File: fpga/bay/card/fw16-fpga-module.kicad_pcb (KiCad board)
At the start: 2 copper layers, 0 parts

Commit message: card PCB: 8-layer 1.2 mm stackup, outline from card-outline.dxf (holes on Dwgs.User), 201 footprints from the schematic; J1 at origin, U14 (rot 90, GT edge to the interposer), H1-H4 per 0012
Co-Authored-By: Claude Opus 5.5 (1M context) <noreply@anthropic.com>
Claude-Session: https://claude.ai/code/session_019QA2U79cSHCaAaMe6Km575
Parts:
- added C1: 10u/25V, Capacitor_SMD:C_1206_3216Metric, F.Cu at (7.30, 28.8)
- added C10: 10u/25V, Capacitor_SMD:C_1206_3216Metric, F.Cu at (7.30, 324.6)
- added C11: 100n/25V, Capacitor_SMD:C_0402_1005Metric, F.Cu at (5.91, 331.2)
- added C12: 100n, Capacitor_SMD:C_0402_1005Metric, F.Cu at (5.91, 337.2)
- added C13: 1u, Capacitor_SMD:C_0402_1005Metric, F.Cu at (5.91, 343.2)
- added C14: 22u/16V, Capacitor_SMD:C_1206_3216Metric, F.Cu at (7.30, 349.9)
- added C15: 22u/16V, Capacitor_SMD:C_1206_3216Metric, F.Cu at (7.30, 357.2)
- added C16: 22u/16V, Capacitor_SMD:C_1206_3216Metric, F.Cu at (7.30, 364.5)
- added C17: 100n, Capacitor_SMD:C_0402_1005Metric, F.Cu at (5.91, 893.7)
- added C18: 100n, Capacitor_SMD:C_0402_1005Metric, F.Cu at (5.91, 500.3)
- added C19: 10u/10V, Capacitor_SMD:C_0805_2012Metric, F.Cu at (6.70, 506.8)
- added C2: 100n, Capacitor_SMD:C_0402_1005Metric, F.Cu at (5.91, 56.0)
- added C20: 10u/10V, Capacitor_SMD:C_0805_2012Metric, F.Cu at (6.70, 513.7)
- added C21: 100n, Capacitor_SMD:C_0402_1005Metric, F.Cu at (5.91, 520.2)
- added C22: 100n, Capacitor_SMD:C_0402_1005Metric, F.Cu at (5.91, 526.2)
- added C23: 1u, Capacitor_SMD:C_0402_1005Metric, F.Cu at (5.91, 532.2)
- added C24: 22u/6.3V, Capacitor_SMD:C_0805_2012Metric, F.Cu at (6.70, 538.7)
- added C25: 22u/6.3V, Capacitor_SMD:C_0805_2012Metric, F.Cu at (6.70, 545.7)
- added C26: 22u/6.3V, Capacitor_SMD:C_0805_2012Metric, F.Cu at (6.70, 552.6)
- added C27: 22u/6.3V, Capacitor_SMD:C_0805_2012Metric, F.Cu at (6.70, 559.6)
- added C28: 10u/10V, Capacitor_SMD:C_0805_2012Metric, F.Cu at (6.70, 566.5)
- added C29: 22u/6.3V, Capacitor_SMD:C_0805_2012Metric, F.Cu at (6.70, 573.5)
- added C3: 1u/25V, Capacitor_SMD:C_0603_1608Metric, F.Cu at (6.48, 279.1)
- added C30: 10u/10V, Capacitor_SMD:C_0805_2012Metric, F.Cu at (6.70, 580.5)
- added C31: 22u/6.3V, Capacitor_SMD:C_0805_2012Metric, F.Cu at (6.70, 587.4)
- added C32: 1u/10V, Capacitor_SMD:C_0402_1005Metric, F.Cu at (5.91, 593.9)
- added C33: 1u, Capacitor_SMD:C_0402_1005Metric, F.Cu at (5.91, 599.9)
- added C34: 1u/10V, Capacitor_SMD:C_0402_1005Metric, F.Cu at (5.91, 605.9)
- added C35: 1u, Capacitor_SMD:C_0402_1005Metric, F.Cu at (5.91, 611.9)
- added C36: 10u/10V, Capacitor_SMD:C_0805_2012Metric, F.Cu at (6.70, 618.4)
- added C37: 1u/10V, Capacitor_SMD:C_0402_1005Metric, F.Cu at (5.91, 624.9)
- added C38: 10n, Capacitor_SMD:C_0402_1005Metric, F.Cu at (5.91, 630.9)
- added C39: 47u/6.3V, Capacitor_SMD:C_1206_3216Metric, F.Cu at (7.30, 637.5)
- added C4: 100n/25V, Capacitor_SMD:C_0402_1005Metric, F.Cu at (5.91, 285.3)
- added C40: 10u/6.3V, Capacitor_SMD:C_0805_2012Metric, F.Cu at (6.70, 644.6)
- added C41: 10u/10V, Capacitor_SMD:C_0805_2012Metric, F.Cu at (6.70, 651.6)
- added C42: 1u/10V, Capacitor_SMD:C_0402_1005Metric, F.Cu at (5.91, 658.1)
- added C43: 10n, Capacitor_SMD:C_0402_1005Metric, F.Cu at (5.91, 664.1)
- added C44: 47u/6.3V, Capacitor_SMD:C_1206_3216Metric, F.Cu at (7.30, 670.7)
- added C45: 10u/6.3V, Capacitor_SMD:C_0805_2012Metric, F.Cu at (6.70, 677.9)
- added C46: 330u/2.5V polymer, Capacitor_Tantalum_SMD:CP_EIA-7343-31_Kemet-D, F.Cu at (9.41, 983.8)
- added C47: 100u/4V, Capacitor_SMD:C_1210_3225Metric, F.Cu at (7.30, 992.8)
- added C48: 47u/4V, Capacitor_SMD:C_1206_3216Metric, F.Cu at (7.30, 1000.6)
- added C49: 47u/4V, Capacitor_SMD:C_1206_3216Metric, F.Cu at (7.30, 1007.9)
- added C5: 10n, Capacitor_SMD:C_0402_1005Metric, F.Cu at (5.91, 291.3)
- added C50: 10u/4V, Capacitor_SMD:C_0603_1608Metric, F.Cu at (6.48, 1014.8)
- added C51: 10u/4V, Capacitor_SMD:C_0603_1608Metric, F.Cu at (6.48, 1021.2)
- added C52: 100n, Capacitor_SMD:C_0402_1005Metric, F.Cu at (5.91, 1027.4)
- added C53: 100n, Capacitor_SMD:C_0402_1005Metric, F.Cu at (5.91, 1033.4)
- added C54: 100n, Capacitor_SMD:C_0402_1005Metric, F.Cu at (5.91, 1039.4)
- added C55: 100n, Capacitor_SMD:C_0402_1005Metric, F.Cu at (5.91, 1045.4)
- added C56: 100n, Capacitor_SMD:C_0402_1005Metric, F.Cu at (5.91, 1051.4)
- added C57: 100n, Capacitor_SMD:C_0402_1005Metric, F.Cu at (5.91, 1057.4)
- added C58: 100n, Capacitor_SMD:C_0402_1005Metric, F.Cu at (5.91, 1063.4)
- added C59: 100n, Capacitor_SMD:C_0402_1005Metric, F.Cu at (5.91, 1069.4)
- added C6: 2.2n, Capacitor_SMD:C_0402_1005Metric, F.Cu at (5.91, 297.3)
- added C60: 47u/4V, Capacitor_SMD:C_1206_3216Metric, F.Cu at (7.30, 1076.1)
- added C61: 10u/4V, Capacitor_SMD:C_0603_1608Metric, F.Cu at (6.48, 1083.0)
- added C62: 10u/4V, Capacitor_SMD:C_0603_1608Metric, F.Cu at (6.48, 1089.4)
- added C63: 47u/4V, Capacitor_SMD:C_1206_3216Metric, F.Cu at (7.30, 1096.3)
- added C64: 47u/4V, Capacitor_SMD:C_1206_3216Metric, F.Cu at (7.30, 1103.6)
- added C65: 10u/4V, Capacitor_SMD:C_0603_1608Metric, F.Cu at (6.48, 1110.5)
- added C66: 10u/4V, Capacitor_SMD:C_0603_1608Metric, F.Cu at (6.48, 1117.0)
- added C67: 10u/4V, Capacitor_SMD:C_0603_1608Metric, F.Cu at (6.48, 1123.4)
- added C68: 10u/4V, Capacitor_SMD:C_0603_1608Metric, F.Cu at (6.48, 1129.9)
- added C69: 10u/4V, Capacitor_SMD:C_0603_1608Metric, F.Cu at (6.48, 1136.3)
- added C7: 10u/25V, Capacitor_SMD:C_1206_3216Metric, F.Cu at (7.30, 304.0)
- added C70: 47u/6.3V, Capacitor_SMD:C_1206_3216Metric, F.Cu at (7.30, 1143.2)
- added C71: 10u/6.3V, Capacitor_SMD:C_0603_1608Metric, F.Cu at (6.48, 1150.1)
- added C72: 4.7u/6.3V, Capacitor_SMD:C_0603_1608Metric, F.Cu at (6.48, 1156.6)
- added C73: 4.7u/6.3V, Capacitor_SMD:C_0603_1608Metric, F.Cu at (6.48, 1163.0)
- added C74: 4.7u/6.3V, Capacitor_SMD:C_0603_1608Metric, F.Cu at (6.48, 1169.5)
- added C75: 470n, Capacitor_SMD:C_0402_1005Metric, F.Cu at (5.91, 1175.7)
- added C76: 100n, Capacitor_SMD:C_0402_1005Metric, F.Cu at (5.91, 1181.7)
- added C77: 220n, Capacitor_SMD:C_0402_1005Metric, F.Cu at (5.91, 1187.7)
- added C78: 220n, Capacitor_SMD:C_0402_1005Metric, F.Cu at (5.91, 1193.7)
- added C79: 220n, Capacitor_SMD:C_0402_1005Metric, F.Cu at (5.91, 1199.7)
- added C8: 100n, Capacitor_SMD:C_0402_1005Metric, F.Cu at (5.91, 310.6)
- added C80: 220n, Capacitor_SMD:C_0402_1005Metric, F.Cu at (5.91, 1205.7)
- added C81: 220n, Capacitor_SMD:C_0402_1005Metric, F.Cu at (5.91, 1211.7)
- added C82: 220n, Capacitor_SMD:C_0402_1005Metric, F.Cu at (5.91, 1217.7)
- added C83: 220n, Capacitor_SMD:C_0402_1005Metric, F.Cu at (5.91, 1223.7)
- added C84: 220n, Capacitor_SMD:C_0402_1005Metric, F.Cu at (5.91, 1229.7)
- added C85: 10n, Capacitor_SMD:C_0402_1005Metric, F.Cu at (5.91, 1235.7)
- added C86: 10n, Capacitor_SMD:C_0402_1005Metric, F.Cu at (5.91, 1241.7)
- added C87: 100n, Capacitor_SMD:C_0402_1005Metric, F.Cu at (5.91, 1247.7)
- added C88: 100n DNP, Capacitor_SMD:C_0402_1005Metric, F.Cu at (5.91, 1253.7)
- added C89: 10n DNP, Capacitor_SMD:C_0402_1005Metric, F.Cu at (5.91, 1259.7)
- added C9: 10u/25V, Capacitor_SMD:C_1206_3216Metric, F.Cu at (7.30, 317.3)
- added C90: 10n DNP, Capacitor_SMD:C_0402_1005Metric, F.Cu at (5.91, 1265.7)
- added D1: green, LED_SMD:LED_0603_1608Metric, F.Cu at (6.48, 1271.9)
- added D2: green, LED_SMD:LED_0603_1608Metric, F.Cu at (6.48, 1278.4)
- added FB1: BLM18PG221SN1, Inductor_SMD:L_0603_1608Metric, F.Cu at (6.48, 1284.9)
- added FB2: BLM18PG221SN1, Inductor_SMD:L_0603_1608Metric, F.Cu at (6.48, 1291.3)
- added H1: M2 SMT nut 9774030243R, fw16-fpga-module:Wurth_WA-SMSI_M2_9774030243R, F.Cu at (-17.5, -52.0)
- added H2: M2 SMT nut 9774030243R, fw16-fpga-module:Wurth_WA-SMSI_M2_9774030243R, F.Cu at (17.5, -52.0)
- added H3: M2 SMT nut 9774030243R, fw16-fpga-module:Wurth_WA-SMSI_M2_9774030243R, F.Cu at (-17.5, -30.1)
- added H4: M2 SMT nut 9774030243R, fw16-fpga-module:Wurth_WA-SMSI_M2_9774030243R, F.Cu at (17.5, -30.1)
- added J1: FXBeam_2x74_DB, fw16-fpga-module:FXBeam_2x74_DB, F.Cu at (0.00, 0.00)
- added J2: AFC58-S04FIA-R1, fw16-fpga-module:AFC58-S04FIA-R1, F.Cu at (8.60, 37.6)
- added J3: AFC58-S04FIA-R1, fw16-fpga-module:AFC58-S04FIA-R1, F.Cu at (8.60, 47.9)
- added J4: TC2050-IDC-NL (Xilinx), Connector:Tag-Connect_TC2050-IDC-NL_2x05_P1.27mm_Vertical, F.Cu at (11.2, 902.6)
- added J5: U.FL PPS/10MHz/trigger, Connector_Coaxial:U.FL_Hirose_U.FL-R-SMT-1_Vertical, F.Cu at (7.17, 1342.8)
- added JP1: WP_EN, Jumper:SolderJumper-2_P1.3mm_Open_Pad1.0x1.5mm, F.Cu at (6.65, 62.7)
- added L1: 10u XAL5030-103, Inductor_SMD:L_Coilcraft_XAL5030-XXX, F.Cu at (7.99, 373.7)
- added L2: 1u XAL4020-102, Inductor_SMD:L_Coilcraft_XAL4020-XXX, F.Cu at (7.40, 686.2)
- added L3: 2.2u DFE201610, Inductor_SMD:L_Murata_DFE201610P, F.Cu at (6.25, 694.7)
- added L4: 2.2u DFE201610, Inductor_SMD:L_Murata_DFE201610P, F.Cu at (6.25, 701.8)
- added Q1: 2N7002K, Package_TO_SOT_SMD:SOT-23, F.Cu at (6.93, 854.1)
- added Q2: 2N7002K, Package_TO_SOT_SMD:SOT-23, F.Cu at (6.93, 862.5)
- added R1: 330k, Resistor_SMD:R_0402_1005Metric, F.Cu at (5.93, 16.2)
- added R10: 1.33k, Resistor_SMD:R_0402_1005Metric, F.Cu at (5.93, 406.3)
- added R11: 390k, Resistor_SMD:R_0402_1005Metric, F.Cu at (5.93, 412.3)
- added R12: 91k, Resistor_SMD:R_0402_1005Metric, F.Cu at (5.93, 418.3)
- added R13: 10k, Resistor_SMD:R_0402_1005Metric, F.Cu at (5.93, 424.3)
- added R14: 10m 1%, Resistor_SMD:R_1206_3216Metric, F.Cu at (7.28, 430.9)
- added R15: 4.7k, Resistor_SMD:R_0402_1005Metric, F.Cu at (5.93, 437.5)
- added R16: 4.7k, Resistor_SMD:R_0402_1005Metric, F.Cu at (5.93, 443.5)
- added R17: 10k, Resistor_SMD:R_0402_1005Metric, F.Cu at (5.93, 449.5)
- added R18: 100k, Resistor_SMD:R_0402_1005Metric, F.Cu at (5.93, 455.5)
- added R19: 24.9k, Resistor_SMD:R_0402_1005Metric, F.Cu at (5.93, 461.5)
- added R2: 330k, Resistor_SMD:R_0402_1005Metric, F.Cu at (5.93, 22.2)
- added R20: 10k, Resistor_SMD:R_0402_1005Metric, F.Cu at (5.93, 467.5)
- added R21: 100k, Resistor_SMD:R_0402_1005Metric, F.Cu at (5.93, 869.7)
- added R22: 100k, Resistor_SMD:R_0402_1005Metric, F.Cu at (5.93, 875.7)
- added R23: 0R, Resistor_SMD:R_0402_1005Metric, F.Cu at (5.93, 881.7)
- added R24: 0R DNP, Resistor_SMD:R_0402_1005Metric, F.Cu at (5.93, 887.7)
- added R25: 2.4k, Resistor_SMD:R_0402_1005Metric, F.Cu at (5.93, 911.4)
- added R26: 4.7k, Resistor_SMD:R_0402_1005Metric, F.Cu at (5.93, 917.4)
- added R27: 4.7k, Resistor_SMD:R_0402_1005Metric, F.Cu at (5.93, 923.4)
- added R28: 4.7k, Resistor_SMD:R_0402_1005Metric, F.Cu at (5.93, 929.4)
- added R29: 4.7k, Resistor_SMD:R_0402_1005Metric, F.Cu at (5.93, 935.4)
- added R3: 10k, Resistor_SMD:R_0402_1005Metric, F.Cu at (5.93, 69.5)
- added R30: 4.7k, Resistor_SMD:R_0402_1005Metric, F.Cu at (5.93, 941.4)
- added R31: 1k, Resistor_SMD:R_0402_1005Metric, F.Cu at (5.93, 947.4)
- added R32: 1k, Resistor_SMD:R_0402_1005Metric, F.Cu at (5.93, 953.4)
- added R33: 1k, Resistor_SMD:R_0402_1005Metric, F.Cu at (5.93, 959.4)
- added R34: 1k, Resistor_SMD:R_0402_1005Metric, F.Cu at (5.93, 965.4)
- added R35: 100k, Resistor_SMD:R_0402_1005Metric, F.Cu at (5.93, 708.4)
- added R36: 100k, Resistor_SMD:R_0402_1005Metric, F.Cu at (5.93, 714.4)
- added R37: 100k, Resistor_SMD:R_0402_1005Metric, F.Cu at (5.93, 720.4)
- added R38: 8.45k 0.1%, Resistor_SMD:R_0402_1005Metric, F.Cu at (5.93, 726.4)
- added R39: 20k 0.1%, Resistor_SMD:R_0402_1005Metric, F.Cu at (5.93, 732.4)
- added R4: 2.2k DNP, Resistor_SMD:R_0402_1005Metric, F.Cu at (5.93, 75.5)
- added R40: 100k, Resistor_SMD:R_0402_1005Metric, F.Cu at (5.93, 738.4)
- added R41: 200k, Resistor_SMD:R_0402_1005Metric, F.Cu at (5.93, 744.4)
- added R42: 100k, Resistor_SMD:R_0402_1005Metric, F.Cu at (5.93, 750.4)
- added R43: 100k, Resistor_SMD:R_0402_1005Metric, F.Cu at (5.93, 756.4)
- added R44: 200k, Resistor_SMD:R_0402_1005Metric, F.Cu at (5.93, 762.4)
- added R45: 120k, Resistor_SMD:R_0402_1005Metric, F.Cu at (5.93, 768.4)
- added R46: 100k, Resistor_SMD:R_0402_1005Metric, F.Cu at (5.93, 774.4)
- added R47: 100k, Resistor_SMD:R_0402_1005Metric, F.Cu at (5.93, 780.4)
- added R48: 100 1%, Resistor_SMD:R_0402_1005Metric, F.Cu at (5.93, 1350.8)
- added R49: 33, Resistor_SMD:R_0402_1005Metric, F.Cu at (5.93, 1356.8)
- added R5: 2.2k DNP, Resistor_SMD:R_0402_1005Metric, F.Cu at (5.93, 81.5)
- added R50: 1k, Resistor_SMD:R_0402_1005Metric, F.Cu at (5.93, 1362.8)
- added R51: 1k, Resistor_SMD:R_0402_1005Metric, F.Cu at (5.93, 1368.8)
- added R6: 390k, Resistor_SMD:R_0402_1005Metric, F.Cu at (5.93, 382.3)
- added R7: 91k, Resistor_SMD:R_0402_1005Metric, F.Cu at (5.93, 388.3)
- added R8: 1M, Resistor_SMD:R_0402_1005Metric, F.Cu at (5.93, 394.3)
- added R9: 57.6k, Resistor_SMD:R_0402_1005Metric, F.Cu at (5.93, 400.3)
- added TP1: VSYS_GPU, TestPoint:TestPoint_Pad_D1.0mm, F.Cu at (6.00, 88.5)
- added TP10: TH_ALERT#, TestPoint:TestPoint_Pad_D1.0mm, F.Cu at (6.00, 160.0)
- added TP11: TH_OVERT#, TestPoint:TestPoint_Pad_D1.0mm, F.Cu at (6.00, 168.0)
- added TP12: I2C_ALW_INT, TestPoint:TestPoint_Pad_D1.0mm, F.Cu at (6.00, 175.9)
- added TP13: GPIO0_EC, TestPoint:TestPoint_Pad_D1.0mm, F.Cu at (6.00, 183.9)
- added TP14: GPIO1_EC, TestPoint:TestPoint_Pad_D1.0mm, F.Cu at (6.00, 191.8)
- added TP15: GPIO2_EC, TestPoint:TestPoint_Pad_D1.0mm, F.Cu at (6.00, 199.8)
- added TP16: GPIO3_EC, TestPoint:TestPoint_Pad_D1.0mm, F.Cu at (6.00, 207.7)
- added TP17: USB_P, TestPoint:TestPoint_Pad_D1.0mm, F.Cu at (6.00, 215.7)
- added TP18: USB_N, TestPoint:TestPoint_Pad_D1.0mm, F.Cu at (6.00, 223.6)
- added TP19: DP_A_AUX, TestPoint:TestPoint_Pad_D1.0mm, F.Cu at (6.00, 231.6)
- added TP2: +5V_ALW, TestPoint:TestPoint_Pad_D1.0mm, F.Cu at (6.00, 96.4)
- added TP20: DP_A_AUX#, TestPoint:TestPoint_Pad_D1.0mm, F.Cu at (6.00, 239.5)
- added TP21: EXT_SSD1_RST#, TestPoint:TestPoint_Pad_D1.0mm, F.Cu at (6.00, 247.5)
- added TP22: EXT_SSD2_RST#, TestPoint:TestPoint_Pad_D1.0mm, F.Cu at (6.00, 255.4)
- added TP23: EXT_SSD2_CLKREQ#, TestPoint:TestPoint_Pad_D1.0mm, F.Cu at (6.00, 263.4)
- added TP3: +3V3_ALW, TestPoint:TestPoint_Pad_D1.0mm, F.Cu at (6.00, 104.4)
- added TP4: +12V_FAN, TestPoint:TestPoint_Pad_D1.0mm, F.Cu at (6.00, 112.3)
- added TP5: GND, TestPoint:TestPoint_Pad_D1.0mm, F.Cu at (6.00, 120.3)
- added TP6: PWR_EN, TestPoint:TestPoint_Pad_D1.0mm, F.Cu at (6.00, 128.2)
- added TP7: PWR_GOOD, TestPoint:TestPoint_Pad_D1.0mm, F.Cu at (6.00, 136.2)
- added TP8: PEX_RST#, TestPoint:TestPoint_Pad_D1.0mm, F.Cu at (6.00, 144.1)
- added TP9: PEX_CLKREQ#, TestPoint:TestPoint_Pad_D1.0mm, F.Cu at (6.00, 152.1)
- added U1: 24LC32, Package_SO:TSSOP-8_4.4x3mm_P0.65mm, F.Cu at (8.85, 271.6)
- added U10: TLV75518PDBV, Package_TO_SOT_SMD:SOT-23-5, F.Cu at (7.05, 817.6)
- added U11: TLV75533PDBV, Package_TO_SOT_SMD:SOT-23-5, F.Cu at (7.05, 826.1)
- added U12: TPS7A8400ARGR, Package_DFN_QFN:QFN-20-1EP_3.5x3.5mm_P0.5mm_EP2x2mm_ThermalVias, F.Cu at (7.38, 835.2)
- added U13: TPS7A8400ARGR, Package_DFN_QFN:QFN-20-1EP_3.5x3.5mm_P0.5mm_EP2x2mm_ThermalVias, F.Cu at (7.38, 845.0)
- added U14: XCAU15P-2FFVB676E, Package_BGA:BGA-676_27.0x27.0mm_Layout26x26_P1.0mm_Ball0.6mm_Pad0.5mm_NSMD, F.Cu at (0.00, -41.0)
- added U15: TPD1E04U04DPY, Package_SON:Texas_DPY0002A_0.6x1mm_P0.65mm, F.Cu at (5.78, 1408.8)
- added U2: TPS259474LRPW, fw16-fpga-module:Texas_RPW0010A_VQFN-HR-10_2x2mm, F.Cu at (6.62, 474.4)
- added U3: INA237AIDGSR, Package_SO:TSSOP-10_3x3mm_P0.5mm, F.Cu at (8.13, 482.5)
- added U4: LMR33630ADDA, Package_SO:Texas_HSOP-8-1EP_3.9x4.9mm_P1.27mm_ThermalVias, F.Cu at (8.75, 492.0)
- added U5: MT25QU256ABA1EW7, Package_DFN_QFN:W-PDFN-8-1EP_6x5mm_P1.27mm_EP3x3mm, F.Cu at (8.80, 973.7)
- added U6: LM3880MF-1AE, Package_TO_SOT_SMD:SOT-23-6, F.Cu at (7.05, 787.7)
- added U7: TPS566238PRQF, fw16-fpga-module:Texas_RQF0009A_VQFN-HR-9_1.5x2mm, F.Cu at (6.62, 795.5)
- added U8: TLV62569PDRL, Package_TO_SOT_SMD:SOT-563, F.Cu at (6.20, 802.7)
- added U9: TLV62569PDRL, Package_TO_SOT_SMD:SOT-563, F.Cu at (6.20, 809.7)
- added Y1: SiT8008 100MHz 3.3V, Oscillator:Oscillator_SMD_SiT_PQFN-4Pin_2.0x1.6mm, F.Cu at (6.50, 1415.6)
- added Y2: SiT9121 100MHz LVDS DNP, Oscillator:Oscillator_SMD_SiTime_SiT9121-6Pin_3.2x2.5mm, F.Cu at (6.53, 1423.7)
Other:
- board outline added: 118.7 x 72.5 mm
- copper layers 2 -> 8

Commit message: card PCB: first placement pass around U14 (bulk decoupling, MGT caps, PCIe AC + refclk caps, RCAL, osc, U.FL, LEDs); 0012 notes
Co-Authored-By: Claude Opus 5.5 (1M context) <noreply@anthropic.com>
Claude-Session: https://claude.ai/code/session_019QA2U79cSHCaAaMe6Km575
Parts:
- moved Y1 1453.7 mm to (24.5, -38.0)
- moved U15 1449.1 mm to (36.0, -40.0)
- moved Y2 1445.8 mm to (16.0, -22.0)
- moved R51 1417.0 mm to (30.0, -48.0)
- moved R50 1409.0 mm to (30.0, -46.0)
- moved R49 1397.0 mm to (33.0, -40.0)
- moved R48 1383.8 mm to (14.3, -33.0), turned to 90 degrees
- moved J5 1383.2 mm to (40.0, -40.0)
- moved D2 1326.7 mm to (33.0, -48.0)
- moved D1 1318.2 mm to (33.0, -46.0)
- moved C87 1284.8 mm to (22.5, -37.0), turned to 90 degrees
- moved C90 1283.8 mm to (16.7, -18.0), turned to 90 degrees
- moved C89 1277.7 mm to (15.5, -18.0), turned to 90 degrees
- moved C88 1275.8 mm to (19.0, -22.0), turned to 90 degrees
- moved C86 1253.7 mm to (13.4, -12.0), turned to 90 degrees
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
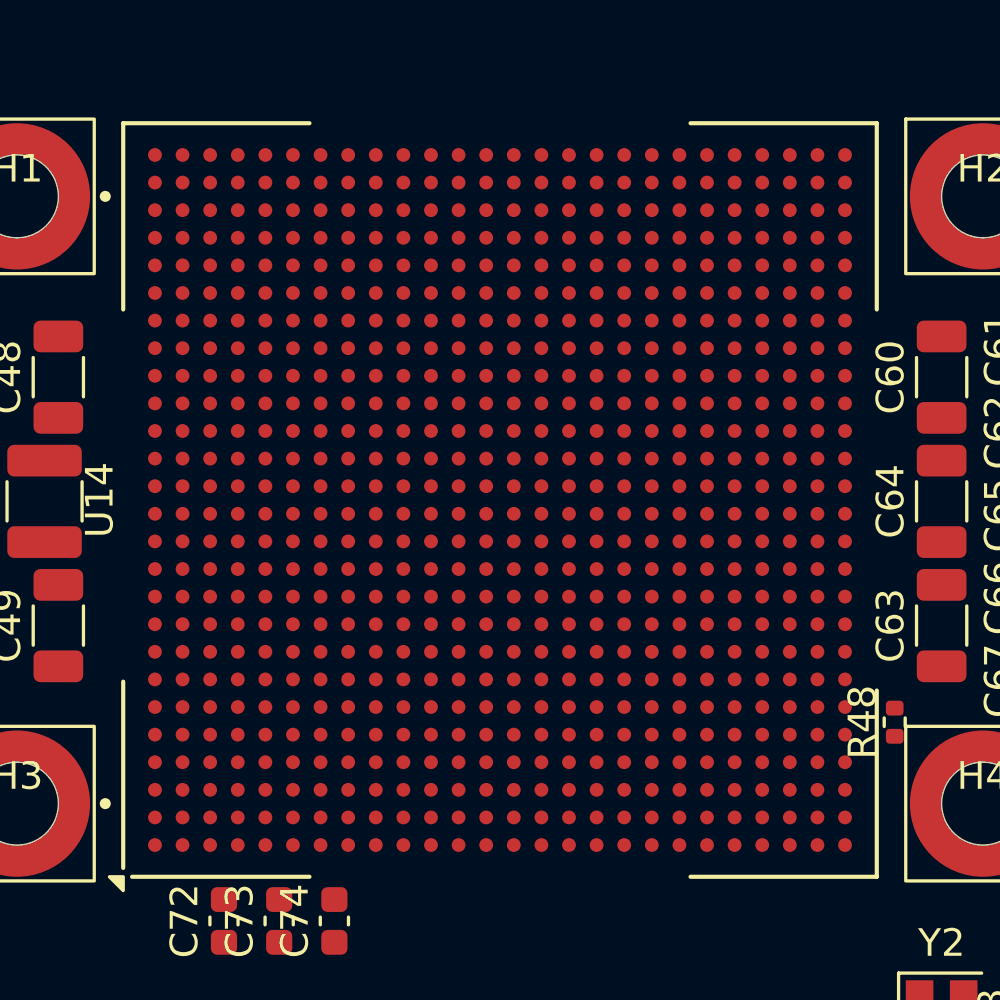
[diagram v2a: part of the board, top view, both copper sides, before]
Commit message: card PCB: U14 selective dogbone fanout applied (288 vias + stubs); 0012 note
Co-Authored-By: Claude Opus 5.5 (1M context) <noreply@anthropic.com>
Claude-Session: https://claude.ai/code/session_019QA2U79cSHCaAaMe6Km575
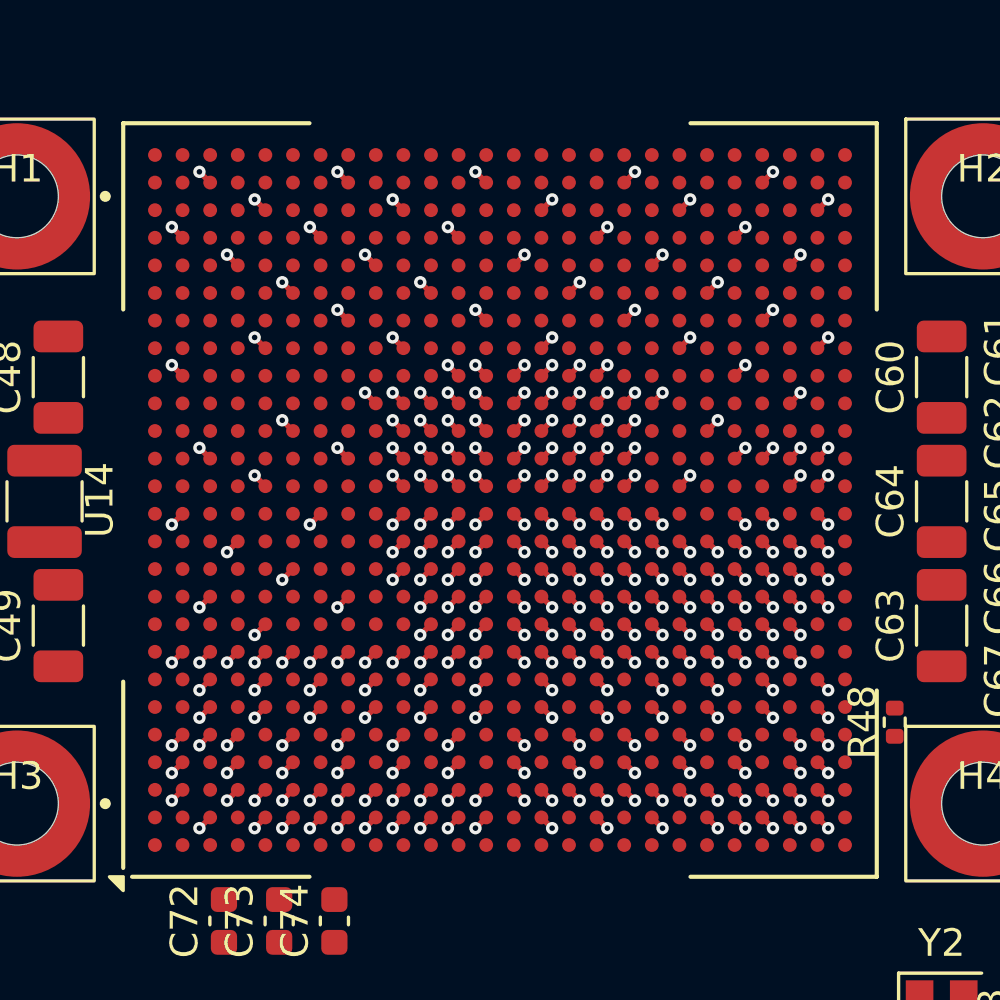
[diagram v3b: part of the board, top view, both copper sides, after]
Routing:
- net GND: track 0.00 -> 95.2 mm, vias 0 -> 173
- net +0V85_VCCINT: track 0.00 -> 22.0 mm, vias 0 -> 40
- net +1V8: track 0.00 -> 11.0 mm, vias 0 -> 20
- net +1V2_MGTAVTT: track 0.00 -> 7.70 mm, vias 0 -> 14
- net +0V9_MGTAVCC: track 0.00 -> 3.30 mm, vias 0 -> 6
- net /FPGA/GNDADC: track 0.00 -> 2.75 mm, vias 0 -> 5
- net +3V3_IO: track 0.00 -> 1.10 mm, vias 0 -> 2
- net +1V8_MGTVCCAUX: track 0.00 -> 1.10 mm, vias 0 -> 2
- net /FPGA/VCCADC: track 0.00 -> 0.55 mm, vias 0 -> 1
- net SENSE_SDA: track 0.00 -> 0.55 mm, vias 0 -> 1
- net SENSE_SCL: track 0.00 -> 0.55 mm, vias 0 -> 1
- net SENSE_ALERT#: track 0.00 -> 0.55 mm, vias 0 -> 1
- net /FPGA/PPS_IN: track 0.00 -> 0.55 mm, vias 0 -> 1
- net FPGA_TDO: track 0.00 -> 0.55 mm, vias 0 -> 1
- net FPGA_PUDC_B: track 0.00 -> 0.55 mm, vias 0 -> 1
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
